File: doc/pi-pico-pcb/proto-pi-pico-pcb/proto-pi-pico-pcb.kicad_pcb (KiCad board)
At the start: 2 copper layers, 26 parts

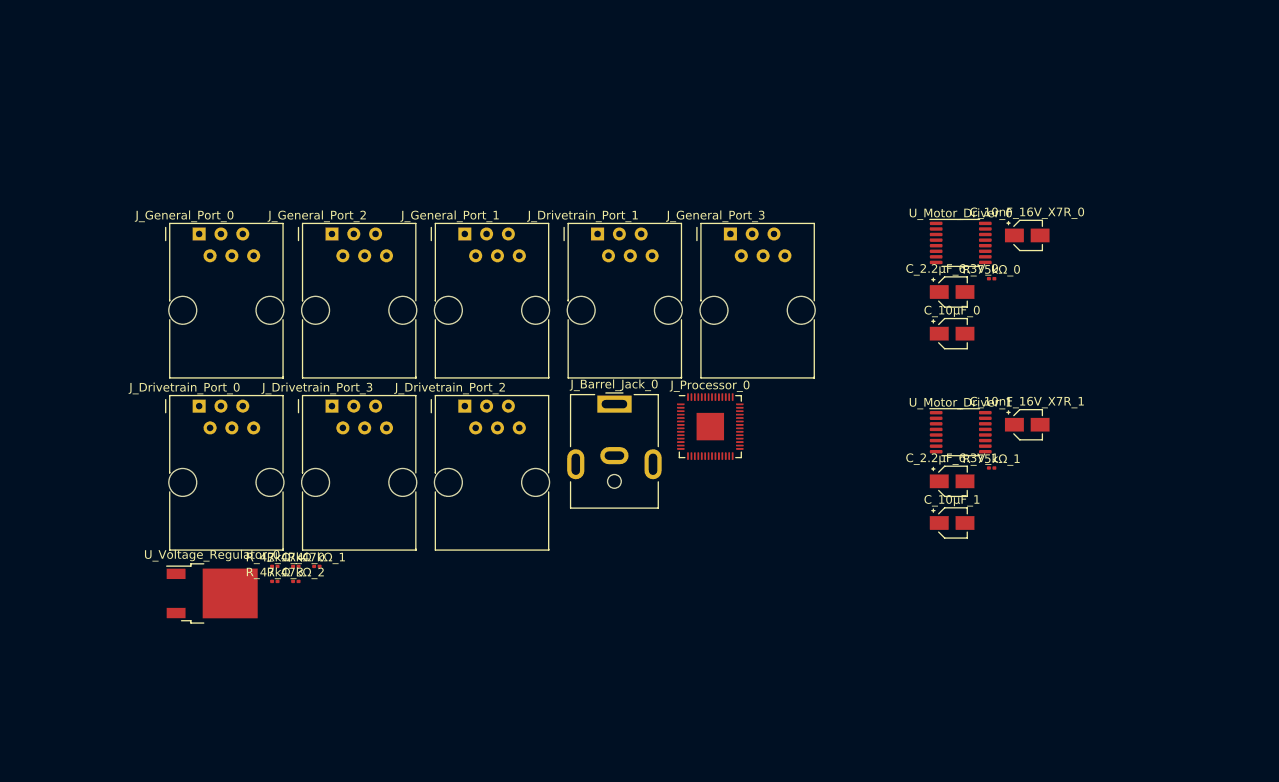
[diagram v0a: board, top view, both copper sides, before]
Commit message: added flash memory
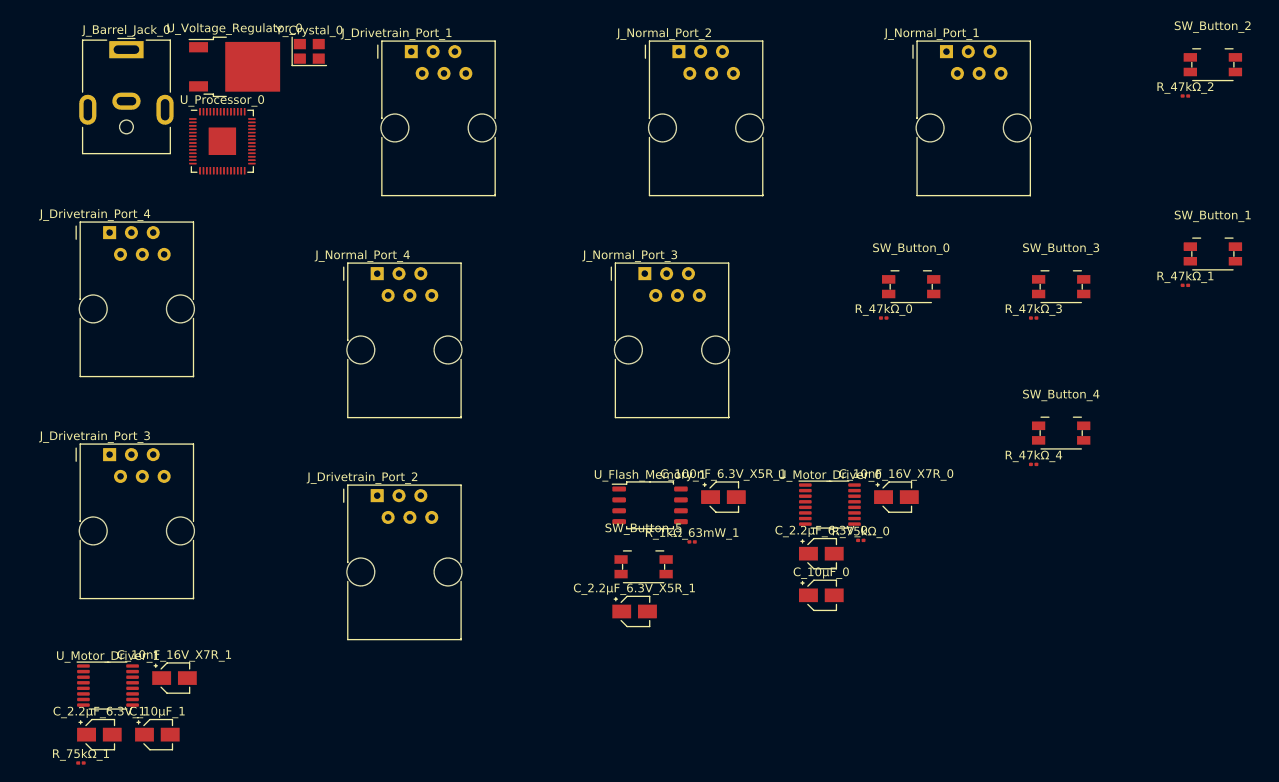
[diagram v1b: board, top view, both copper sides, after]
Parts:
- removed J_Drivetrain_Port_0, J_General_Port_0, J_General_Port_1, J_General_Port_2, J_General_Port_3: 6P6C, Connector_RJ:RJ12_Amphenol_54601
- removed J_Processor_0: RP2040, Package_DFN_QFN:QFN-56-1EP_7x7mm_P0.4mm_EP3.2x3.2mm
- added C_100nF_6.3V_X5R_1: C, Capacitor_SMD:CP_Elec_3x5.3, F.Cu at (148.6, 112.8)
- added C_2.2μF_6.3V_X5R_1: C, Capacitor_SMD:CP_Elec_3x5.3, F.Cu at (138.3, 126.1)
- added J_Drivetrain_Port_4: 6P6C, Connector_RJ:RJ12_Amphenol_54601, F.Cu at (77.1, 82.0)
- added J_Normal_Port_1: 6P6C, Connector_RJ:RJ12_Amphenol_54601, F.Cu at (174.6, 60.9)
- added J_Normal_Port_2: 6P6C, Connector_RJ:RJ12_Amphenol_54601, F.Cu at (143.4, 60.9)
- added J_Normal_Port_3: 6P6C, Connector_RJ:RJ12_Amphenol_54601, F.Cu at (139.5, 86.8)
- added J_Normal_Port_4: 6P6C, Connector_RJ:RJ12_Amphenol_54601, F.Cu at (108.3, 86.8)
- added R_1kΩ_63mW_1: R, Resistor_SMD:R_0201_0603Metric, F.Cu at (145.0, 118.0)
- added SW_Button_0: SW_Push, Button_Switch_SMD:Panasonic_EVQPUJ_EVQPUA, F.Cu at (170.5, 88.3)
- added SW_Button_1: SW_Push, Button_Switch_SMD:Panasonic_EVQPUJ_EVQPUA, F.Cu at (205.6, 84.5)
- added SW_Button_2: SW_Push, Button_Switch_SMD:Panasonic_EVQPUJ_EVQPUA, F.Cu at (205.6, 62.4)
- added SW_Button_3: SW_Push, Button_Switch_SMD:Panasonic_EVQPUJ_EVQPUA, F.Cu at (188.0, 88.3)
- added SW_Button_4: SW_Push, Button_Switch_SMD:Panasonic_EVQPUJ_EVQPUA, F.Cu at (188.0, 105.3)
- added SW_Button_5: SW_Push, Button_Switch_SMD:Panasonic_EVQPUJ_EVQPUA, F.Cu at (139.3, 120.9)
- added U_Flash_Memory_1: W25Q32JVSS, Package_SO:SOIC-8_5.23x5.23mm_P1.27mm, F.Cu at (140.1, 113.8)
- added U_Processor_0: RP2040, Package_DFN_QFN:QFN-56-1EP_7x7mm_P0.4mm_EP3.2x3.2mm, F.Cu at (90.2, 71.3)
- added Y_Crystal_0: Crystal, Crystal:Crystal_SMD_Abracon_ABM8G-4Pin_3.2x2.5mm, F.Cu at (100.4, 60.9)
- moved R_47kΩ_2 118.0 mm to (202.4, 66.1)
- moved R_75kΩ_1 111.5 mm to (73.8, 143.8)
- moved R_47kΩ_1 106.3 mm to (202.4, 88.1)
- moved C_10nF_16V_X7R_1 103.6 mm to (84.7, 133.9)
- moved C_2.2μF_6.3V_1 103.6 mm to (75.9, 140.5)
- moved U_Motor_Driver_1 103.6 mm to (76.9, 134.7)
- moved C_10μF_1 95.8 mm to (82.7, 140.5)
- moved R_47kΩ_3 93.6 mm to (184.8, 91.9)
- moved R_47kΩ_4 89.2 mm to (184.8, 109.0)
- moved R_47kΩ_0 74.3 mm to (167.3, 91.9)
- moved J_Barrel_Jack_0 70.3 mm to (79.1, 60.7)
- moved U_Voltage_Regulator_0 61.4 mm to (91.7, 62.7)
- moved R_75kΩ_0 34.1 mm to (164.6, 117.8)
- moved C_10nF_16V_X7R_0 34.1 mm to (168.8, 112.8)
- moved C_10μF_0 34.1 mm to (160.0, 124.2)
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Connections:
- J_Drivetrain_Port_1 pad 1: /Motor_Driver_Sheet_0/BOUT2 -> GND
- J_Drivetrain_Port_1 pad 2: /Motor_Driver_Sheet_0/BOUT1 -> +3.3V
- J_Drivetrain_Port_1 pad 3: /DP11 -> /GP_10
- J_Drivetrain_Port_1 pad 4: /DP10 -> /GP_11
- J_Drivetrain_Port_1 pad 5: +3.3V -> /Drivetrain_Port_1/DC_0
- J_Drivetrain_Port_1 pad 6: GND -> /Drivetrain_Port_1/DC_1
- J_Drivetrain_Port_2 pad 1: /Motor_Driver_Sheet_1/AOUT2 -> GND
- J_Drivetrain_Port_2 pad 2: /Motor_Driver_Sheet_1/AOUT1 -> +3.3V
- J_Drivetrain_Port_2 pad 3: /DP21 -> /GP_14
- J_Drivetrain_Port_2 pad 4: /DP20 -> /GP_15
- J_Drivetrain_Port_2 pad 5: +3.3V -> /Drivetrain_Port_3/DC_0
- J_Drivetrain_Port_2 pad 6: GND -> /Drivetrain_Port_3/DC_1
- J_Drivetrain_Port_3 pad 1: /Motor_Driver_Sheet_1/BOUT2 -> GND
- J_Drivetrain_Port_3 pad 2: /Motor_Driver_Sheet_1/BOUT1 -> +3.3V
- J_Drivetrain_Port_3 pad 3: /DP31 -> /GP_12
- J_Drivetrain_Port_3 pad 4: /DP30 -> /GP_13
- J_Drivetrain_Port_3 pad 5: +3.3V -> /Drivetrain_Port_2/DC_0
- J_Drivetrain_Port_3 pad 6: GND -> /Drivetrain_Port_2/DC_1
- R_47kΩ_0 pad 2: Net-(J_Processor_0-Pad26) -> /GP_0
- R_47kΩ_1 pad 1: Net-(J_Processor_0-Pad38) -> +3.3V
- R_47kΩ_1 pad 2: +3.3V -> /GP_1
- R_47kΩ_2 pad 1: Net-(J_Processor_0-Pad39) -> +3.3V
- R_47kΩ_2 pad 2: +3.3V -> /GP_2
- R_47kΩ_3 pad 1: Net-(J_Processor_0-Pad40) -> +3.3V
- R_47kΩ_3 pad 2: +3.3V -> /GP_3
- R_47kΩ_4 pad 1: Net-(J_Processor_0-Pad41) -> +3.3V
- R_47kΩ_4 pad 2: +3.3V -> /RESET_Button_0/SIGNAL
- U_Motor_Driver_0 pad 10: /Motor_Driver_Sheet_0/BIN2 -> /Motor_Driver_0/B_IN_1
- U_Motor_Driver_0 pad 15: /Motor_Driver_Sheet_0/AIN2 -> /Motor_Driver_0/A_IN_1
- U_Motor_Driver_0 pad 16: /Motor_Driver_Sheet_0/AIN1 -> /Motor_Driver_0/A_IN_0
- U_Motor_Driver_0 pad 2: /Motor_Driver_Sheet_0/AOUT1 -> /Drivetrain_Port_0/DC_0
- U_Motor_Driver_0 pad 4: /Motor_Driver_Sheet_0/AOUT2 -> /Drivetrain_Port_0/DC_1
- U_Motor_Driver_0 pad 5: /Motor_Driver_Sheet_0/BOUT2 -> /Drivetrain_Port_1/DC_1
- U_Motor_Driver_0 pad 7: /Motor_Driver_Sheet_0/BOUT1 -> /Drivetrain_Port_1/DC_0
- U_Motor_Driver_0 pad 9: /Motor_Driver_Sheet_0/BIN1 -> /Motor_Driver_0/B_IN_0
- U_Motor_Driver_1 pad 10: /Motor_Driver_Sheet_1/BIN2 -> /Motor_Driver_1/B_IN_1
- U_Motor_Driver_1 pad 15: /Motor_Driver_Sheet_1/AIN2 -> /Motor_Driver_1/A_IN_1
- U_Motor_Driver_1 pad 16: /Motor_Driver_Sheet_1/AIN1 -> /Motor_Driver_1/A_IN_0
- U_Motor_Driver_1 pad 2: /Motor_Driver_Sheet_1/AOUT1 -> /Drivetrain_Port_2/DC_0
- U_Motor_Driver_1 pad 4: /Motor_Driver_Sheet_1/AOUT2 -> /Drivetrain_Port_2/DC_1
- U_Motor_Driver_1 pad 5: /Motor_Driver_Sheet_1/BOUT2 -> /Drivetrain_Port_3/DC_1
- U_Motor_Driver_1 pad 7: /Motor_Driver_Sheet_1/BOUT1 -> /Drivetrain_Port_3/DC_0
- U_Motor_Driver_1 pad 9: /Motor_Driver_Sheet_1/BIN1 -> /Motor_Driver_1/B_IN_0
